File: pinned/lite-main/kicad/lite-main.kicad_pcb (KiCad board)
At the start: 2 copper layers, 100 x 90 mm, 138 parts, among them J1 USB4105-GF-A-120, J2 RCA line in, J3 RCA sub out, J4 DB128V-5.08-4P, Q1 AO4485, Q2 MMBT3904, Q3 MMBT3904, Q4 MMBT3904, SW1 TS-1187A, SW2 TS-1187A, SW3 TS-1187A, U1 CH224A, U2 TPS54302, U3 SY8089A1AAC, U4 LP5907-3.3, U5 ESP32-WROVER-E-N8R8, U6 CH340C, U7 ES8388, U8 TPA3118D2, U9 IRM-3638T

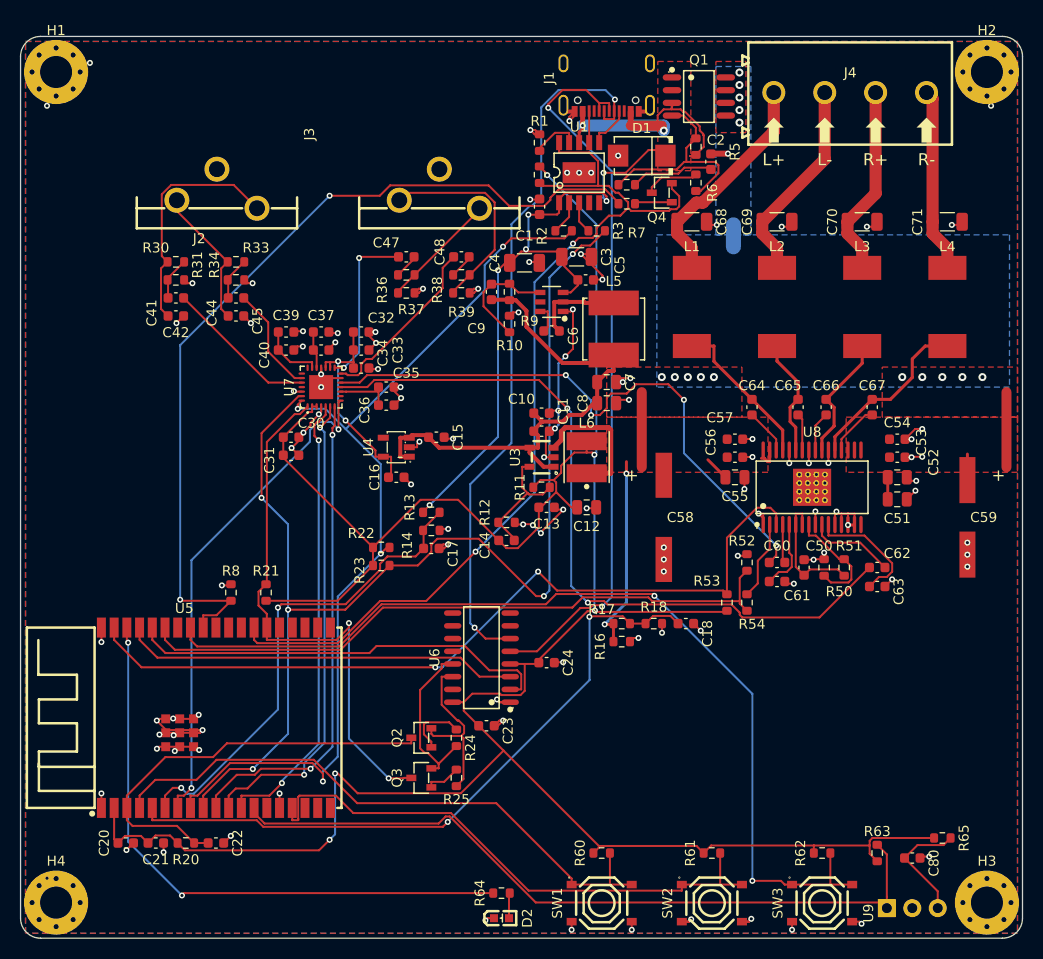
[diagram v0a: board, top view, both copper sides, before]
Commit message: hwde's score reads the hi-fi boards as they are now: re-pin core and lite-main at hifi-receiver-2 main, add ultra-front
* hwde's score reads the hi-fi boards as they are now: core and lite-ma…

…in re-pinned at hifi-receiver-2 56e91aa, ultra-front added

The re-pin is a new baseline (docs/score.md): 9da177ca's review-2 ECO scripts are
classified as stand-ins with the gap each fills.

* merge main
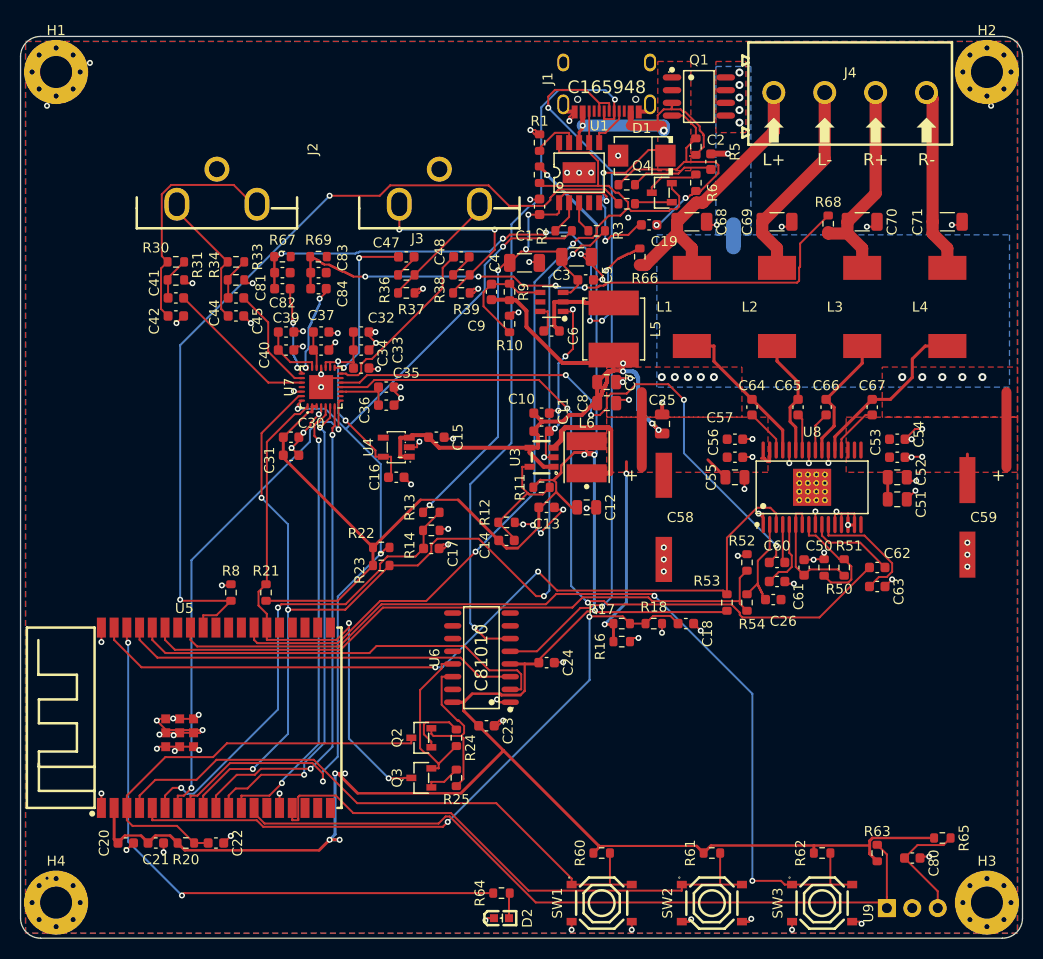
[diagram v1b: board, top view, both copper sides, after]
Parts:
- added C19: 4.7uF, Capacitor_SMD:C_0603_1608Metric, F.Cu at (85.6, 79.1)
- added C25: 22uF, Capacitor_SMD:C_0805_2012Metric, F.Cu at (86.9, 99.0)
- added C26: 47nF, Capacitor_SMD:C_0603_1608Metric, F.Cu at (98.0, 116.5)
- added C81: 470pF, Capacitor_SMD:C_0603_1608Metric, F.Cu at (49.0, 83.9)
- added C82: 1uF, Capacitor_SMD:C_0603_1608Metric, F.Cu at (49.0, 85.5)
- added C83: 470pF, Capacitor_SMD:C_0603_1608Metric, F.Cu at (52.6, 83.9)
- added C84: 1uF, Capacitor_SMD:C_0603_1608Metric, F.Cu at (52.6, 85.5)
- added R66: 100k, Resistor_SMD:R_0603_1608Metric, F.Cu at (84.7, 82.3)
- added R67: 10k, Resistor_SMD:R_0603_1608Metric, F.Cu at (49.0, 82.3)
- added R68: 100k, Resistor_SMD:R_0603_1608Metric, F.Cu at (103.5, 79.0)
- added R69: 10k, Resistor_SMD:R_0603_1608Metric, F.Cu at (52.6, 82.3)
- C9: value 100pF -> 47pF
- J1: value USB4105-GF-A-120 -> TYPE-C-31-M-12; footprint aiee:USB-C-SMD_MC-311D -> aiee:USB-C_SMD-TYPE-C-31-M-12_1
- R30, R33: value 10k -> 15k
- R54: value 100k -> 10k
- R6: value 47k -> 220k
- U6: value CH340C -> CH340B
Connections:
- U7 pad 21: unconnected-(U7-RIN2-Pad21) -> /TAP_R_C
- U7 pad 22: unconnected-(U7-LIN2-Pad22) -> /TAP_L_C
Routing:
- net /TAP_R: track 0.00 -> 61.2 mm, vias 0 -> 4
- net /TAP_L: track 0.00 -> 54.2 mm, vias 0 -> 6
- net +5V: track 52.8 -> 68.9 mm, vias 0 -> 4
- net /TAP_L_C: track 0.00 -> 8.99 mm, vias 0 -> 2
- net /TAP_R_C: track 0.00 -> 8.98 mm, vias 0 -> 2
- net VBUS: track 91.7 -> 100.5 mm, vias 8 -> 9
- net +3V3: track 264.9 -> 271.1 mm, vias 5 -> 8
- net /PSW_G: track 21.5 -> 27.3 mm, vias 0 -> 2
- net /SPK_L_P: track 22.5 -> 27.5 mm
- net /SPK_R_P: track 19.3 -> 21.3 mm
- net /AMP_SDZ: track 7.90 -> 9.85 mm
- net /USB_DM: track 71.4 -> 73.0 mm
- net GND: track 162.1 -> 163.3 mm, vias 115 -> 117
- net /USB_DP: track 73.1 -> 73.9 mm
- net /SUB_R: track 21.0 -> 21.1 mm, vias 0 -> 2
